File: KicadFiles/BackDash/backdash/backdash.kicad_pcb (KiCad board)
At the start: 2 copper layers, 7 parts

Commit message: need to add in power
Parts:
- removed NANO4: Conn_01x30_Female, TestBaja:arduino_nano
- added REF**: Pin_Header_Straight_1x03_Pitch2.54mm, Pin_Headers:Pin_Header_Straight_1x03_Pitch2.54mm, F.Cu at (231.1, 29.2)
- added REF**: Pin_Header_Straight_1x03_Pitch2.54mm, Pin_Headers:Pin_Header_Straight_1x03_Pitch2.54mm, F.Cu at (219.7, 27.9)
- added REF**: Pin_Header_Straight_1x04_Pitch2.54mm, Pin_Headers:Pin_Header_Straight_1x04_Pitch2.54mm, F.Cu at (247.7, 27.9)
- moved NANO3 188.1 mm to (242.6, 64.8), turned to 270 degrees
- moved NANO2 112.6 mm to (189.2, 50.8), turned to 180 degrees
- moved BUCK1 106.6 mm to (213.4, 41.9), turned to 270 degrees
- moved RTD1 90.7 mm to (193.0, 86.4), turned to 90 degrees
- moved NANO1 80.8 mm to (189.2, 31.8), turned to 180 degrees
- moved CAN1 20.7 mm to (232.4, 86.4), turned to 90 degrees
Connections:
- net /INT renamed Net-(CAN1-Pad10)
- net /RDY renamed Net-(RTD1-Pad8)
- net Net-(BUCK1-Pad3) renamed /IN
- BUCK1 pad 4: Net-(BUCK1-Pad4) -> /GND
- BUCK1 pad 5: Net-(BUCK1-Pad5) -> /VCC
- CAN1 pad 1: /GND -> Net-(CAN1-Pad1)
- CAN1 pad 11: /NC -> Net-(CAN1-Pad11)
- CAN1 pad 12: /NC -> Net-(CAN1-Pad12)
- CAN1 pad 13: /NC -> Net-(CAN1-Pad13)
- CAN1 pad 14: /NC -> Net-(CAN1-Pad14)
- CAN1 pad 2: /3.3V -> /3V3
- CAN1 pad 4: /SDO -> /SDOcan
- CAN1 pad 6: /CS -> /CScan
- CAN1 pad 7: /RST -> Net-(CAN1-Pad7)
- CAN1 pad 8: /NC -> Net-(CAN1-Pad8)
- CAN1 pad 9: /NC -> Net-(CAN1-Pad9)
- NANO1 pad 1: /TX1 -> Net-(NANO1-Pad1)
- NANO1 pad 10: /D7 -> Net-(NANO1-Pad10)
- NANO1 pad 11: /D8 -> Net-(NANO1-Pad11)
- NANO1 pad 12: /D9 -> Net-(NANO1-Pad12)
- NANO1 pad 13: /D10 -> Net-(NANO1-Pad13)
- NANO1 pad 14: /D11 -> Net-(NANO1-Pad14)
- NANO1 pad 15: /D12 -> Net-(NANO1-Pad15)
- NANO1 pad 16: /D13 -> Net-(NANO1-Pad16)
- NANO1 pad 17: /3.3V -> Net-(NANO1-Pad17)
- NANO1 pad 18: /REF -> Net-(NANO1-Pad18)
- NANO1 pad 2: /RX0 -> Net-(NANO1-Pad2)
- NANO1 pad 20: /A1 -> Net-(NANO1-Pad20)
- NANO1 pad 21: /A2 -> Net-(NANO1-Pad21)
- NANO1 pad 22: /A3 -> Net-(NANO1-Pad22)
- NANO1 pad 25: /A6 -> Net-(NANO1-Pad25)
- NANO1 pad 26: /A7 -> Net-(NANO1-Pad26)
- NANO1 pad 28: /RST -> Net-(NANO1-Pad28)
- NANO1 pad 3: /RST -> Net-(NANO1-Pad3)
- NANO1 pad 30: /VIN -> Net-(NANO1-Pad30)
- NANO1 pad 4: /GND -> Net-(NANO1-Pad4)
- NANO1 pad 5: /D2 -> Net-(NANO1-Pad5)
- NANO1 pad 6: /D3 -> Net-(NANO1-Pad6)
- NANO1 pad 7: /D4 -> Net-(NANO1-Pad7)
- NANO1 pad 8: /D5 -> Net-(NANO1-Pad8)
- NANO1 pad 9: /D6 -> Net-(NANO1-Pad9)
- NANO2 pad 1: /TX1 -> Net-(NANO2-Pad1)
- NANO2 pad 10: /D7 -> Net-(NANO2-Pad10)
- NANO2 pad 11: /D8 -> Net-(NANO2-Pad11)
- NANO2 pad 12: /D9 -> /CSrtd
- NANO2 pad 14: /D11 -> /CLK
- NANO2 pad 15: /D12 -> /SDOrtd
- NANO2 pad 16: /D13 -> /CLK
- NANO2 pad 17: /3.3V -> Net-(NANO2-Pad17)
- NANO2 pad 18: /REF -> Net-(NANO2-Pad18)
- NANO2 pad 19: /A0 -> Net-(NANO2-Pad19)
- NANO2 pad 2: /RX0 -> Net-(NANO2-Pad2)
- NANO2 pad 20: /A1 -> Net-(NANO2-Pad20)
- NANO2 pad 21: /A2 -> Net-(NANO2-Pad21)
- NANO2 pad 22: /A3 -> Net-(NANO2-Pad22)
- NANO2 pad 25: /A6 -> Net-(NANO2-Pad25)
- NANO2 pad 26: /A7 -> Net-(NANO2-Pad26)
- NANO2 pad 28: /RST -> Net-(NANO2-Pad28)
- NANO2 pad 3: /RST -> Net-(NANO2-Pad3)
- NANO2 pad 30: /VIN -> Net-(NANO2-Pad30)
- NANO2 pad 4: /GND -> Net-(NANO2-Pad4)
- NANO2 pad 5: /D2 -> Net-(NANO2-Pad5)
- NANO2 pad 6: /D3 -> Net-(NANO2-Pad6)
- NANO2 pad 7: /D4 -> Net-(NANO2-Pad7)
- NANO2 pad 8: /D5 -> Net-(NANO2-Pad8)
- NANO2 pad 9: /D6 -> Net-(NANO2-Pad9)
- NANO3 pad 1: /TX1 -> Net-(NANO3-Pad1)
- NANO3 pad 10: /D7 -> Net-(NANO3-Pad10)
- NANO3 pad 11: /D8 -> Net-(NANO3-Pad11)
- NANO3 pad 12: /D9 -> Net-(NANO3-Pad12)
- NANO3 pad 13: /D10 -> /CScan
- NANO3 pad 14: /D11 -> /SDI
- NANO3 pad 15: /D12 -> /SDOcan
- NANO3 pad 16: /D13 -> /SCK
- NANO3 pad 17: /3.3V -> Net-(NANO3-Pad17)
- NANO3 pad 18: /REF -> Net-(NANO3-Pad18)
- NANO3 pad 19: /A0 -> Net-(NANO3-Pad19)
- NANO3 pad 2: /RX0 -> Net-(NANO3-Pad2)
- NANO3 pad 20: /A1 -> Net-(NANO3-Pad20)
- NANO3 pad 21: /A2 -> Net-(NANO3-Pad21)
- NANO3 pad 22: /A3 -> Net-(NANO3-Pad22)
- NANO3 pad 25: /A6 -> Net-(NANO3-Pad25)
- NANO3 pad 26: /A7 -> Net-(NANO3-Pad26)
- NANO3 pad 28: /RST -> Net-(NANO3-Pad28)
- NANO3 pad 3: /RST -> Net-(NANO3-Pad3)
- NANO3 pad 30: /VIN -> Net-(NANO3-Pad30)
- NANO3 pad 4: /GND -> Net-(NANO3-Pad4)
- NANO3 pad 5: /D2 -> Net-(NANO3-Pad5)
- NANO3 pad 6: /D3 -> Net-(NANO3-Pad6)
- NANO3 pad 7: /D4 -> Net-(NANO3-Pad7)
- NANO3 pad 8: /D5 -> Net-(NANO3-Pad8)
- NANO3 pad 9: /D6 -> Net-(NANO3-Pad9)
- RTD1 pad 3: /3V3 -> Net-(RTD1-Pad3)
- RTD1 pad 5: /SDO -> /SDOrtd
- RTD1 pad 7: /CS -> /CSrtd
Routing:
- net /VCC: track 0.00 -> 169.4 mm
- net /A4: track 0.00 -> 124.9 mm
- net /A5: track 0.00 -> 115.6 mm
- net /SDI: track 0.00 -> 67.3 mm
- net /CLK: track 0.00 -> 52.4 mm
- net /GND: track 0.00 -> 52.0 mm
- net /A0: track 0.00 -> 44.3 mm
- net /SDOrtd: track 0.00 -> 39.4 mm
- net /SCK: track 0.00 -> 36.0 mm
- net /CSrtd: track 0.00 -> 29.0 mm
- net /CScan: track 0.00 -> 22.2 mm
- net /SDOcan: track 0.00 -> 15.0 mm
- added copper zone on B.Cu, net /GND
- added copper zone on F.Cu, net /VCC
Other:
- board outline added: 91.4 x 67.3 mm
- net class Default: trace_width 0.25 -> 0.508
- board text added: "cvt"
- board text added: "tach"

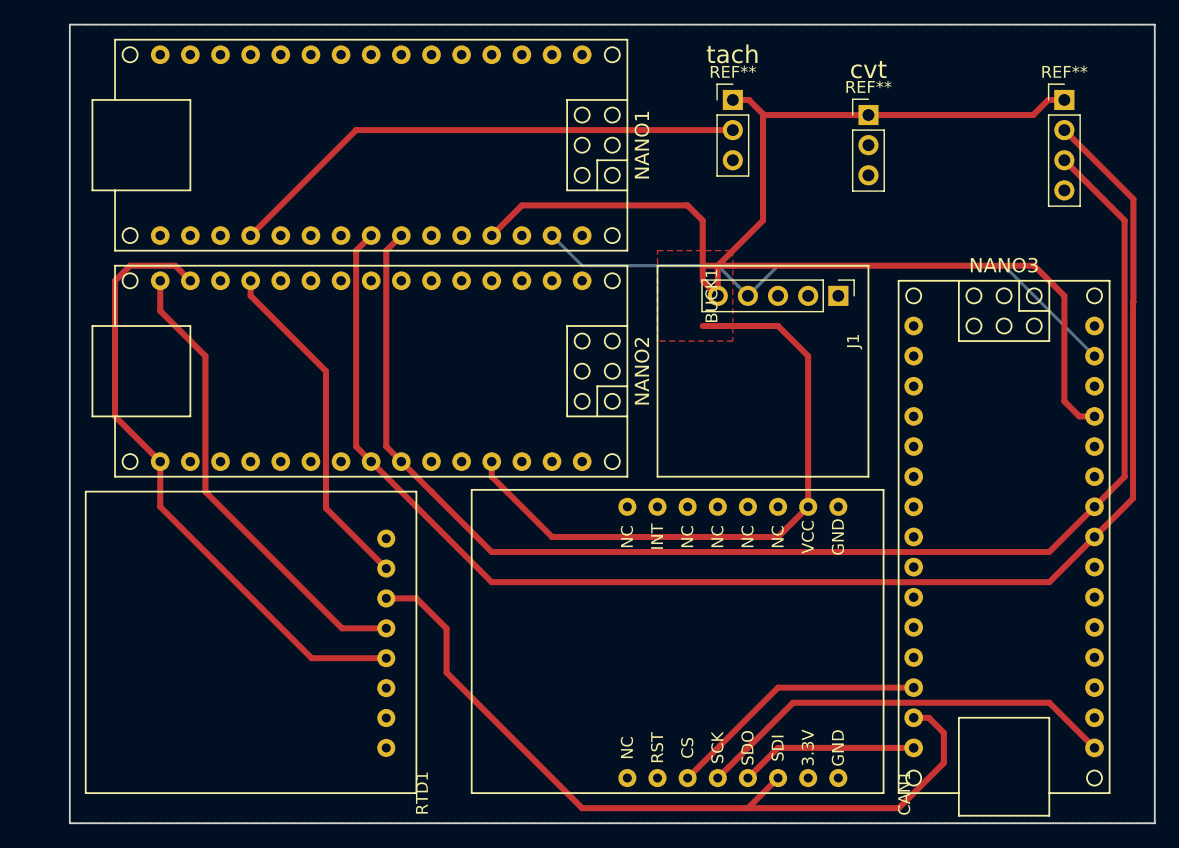
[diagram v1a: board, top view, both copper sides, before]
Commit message: logo and batt added
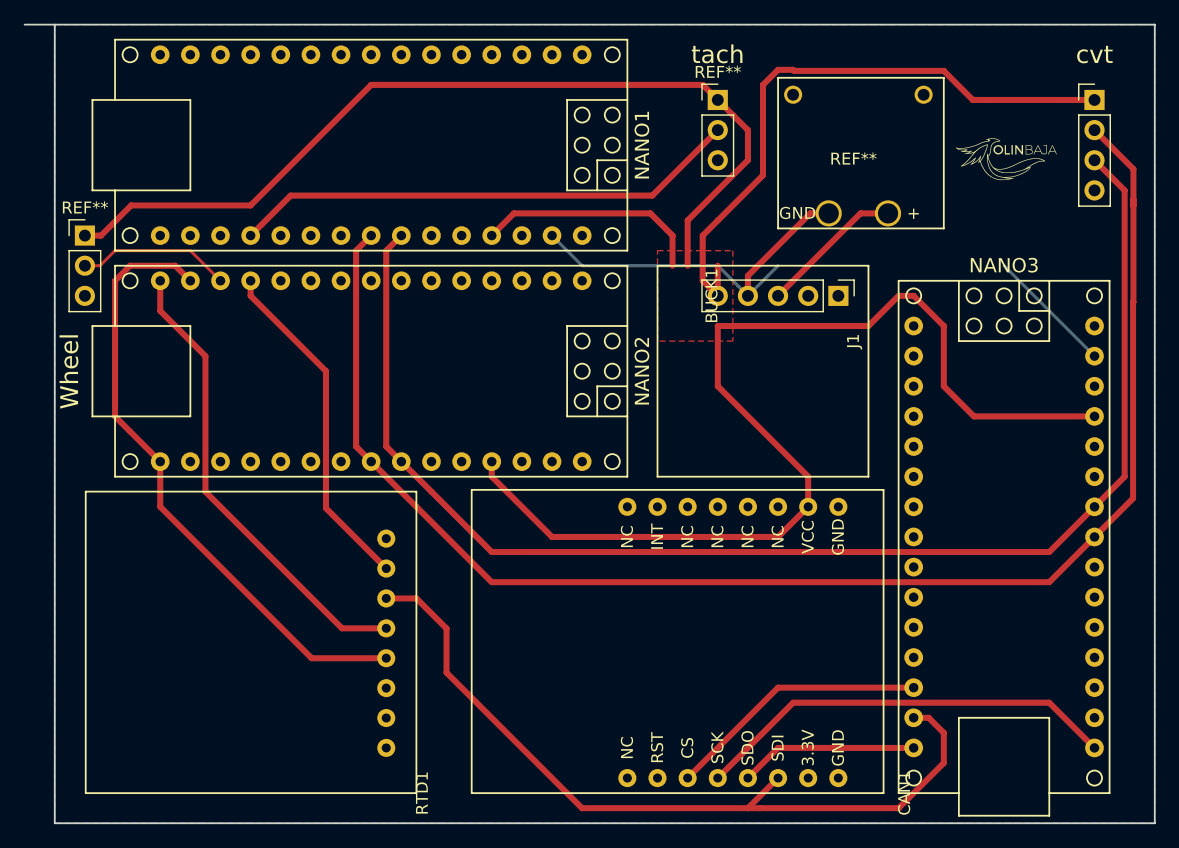
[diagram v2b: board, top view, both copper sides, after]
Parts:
- added G***: LOGO, TestBaja:Baja_Logo_Tach, F.Cu at (243.8, 33.0)
- added REF**: DC_Connector, TestBaja:DC_Connector, F.Cu at (224.8, 37.5)
- moved REF** 66.8 mm to (165.1, 39.4)
- moved REF** 2.54 mm to (250.2, 27.9)
- moved REF** 1.27 mm to (218.4, 27.9)
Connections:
- REF** pad 2: (no net) -> /D10
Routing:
- net /VCC: track 169.4 -> 237.5 mm
- net /D10: track 0.00 -> 13.0 mm
- net /IN: track 0.00 -> 12.1 mm
- net /GND: track 52.0 -> 43.7 mm
- net /A0: track 44.3 -> 43.1 mm
- net /A5: track 115.6 -> 114.6 mm
- net /A4: track 124.9 -> 124.4 mm
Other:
- board size 91.4 x 67.3 mm -> 95.2 x 67.3 mm
- board text added: "Wheel"

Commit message: Board edge was a little off
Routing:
- net /CLK: track 52.4 -> 53.7 mm
- net /D10: track 13.0 -> 14.0 mm
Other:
- board size 95.2 x 67.3 mm -> 92.7 x 67.3 mm
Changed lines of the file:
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@@
-(kicad_pcb (version 20171130) (host pcbnew 6.0.0-rc1-unknown-7c960aa~66~ubuntu18.04.1)
+(kicad_pcb (version 20171130) (host pcbnew "(5.0.0)")
   (general
     (thickness 1.6)
     (drawings 7)
-    (tracks 126)
+    (tracks 129)
     (zones 0)
     (modules 11)
@@
     (zone_45_only no)
     (trace_min 0.2)
+    (segment_width 0.2)
+    (edge_width 0.15)
     (via_size 0.8)
     (via_drill 0.4)
@@
     (uvia_min_size 0.2)
     (uvia_min_drill 0.1)
-    (edge_width 0.15)
-    (segment_width 0.2)
     (pcb_text_width 0.3)
     (pcb_text_size 1.5 1.5)
@@
     (pcbplotparams
       (layerselection 0x010fc_ffffffff)
-      (usegerberextensions false)
+      (usegerberextensions true)
       (usegerberattributes false)
       (usegerberadvancedattributes false)
@@
       (outputformat 1)
       (mirror false)
-      (drillshape 1)
+      (drillshape 0)
       (scaleselection 1)
-      (outputdirectory ""))
+      (outputdirectory "../../BackDashv1_gerbers/"))
   )
   (net 0 "")
@@
   (gr_line (start 255.27 88.9) (end 162.56 88.9) (layer Edge.Cuts) (width 0.15))
   (gr_line (start 255.27 21.59) (end 255.27 88.9) (layer Edge.Cuts) (width 0.15))
-  (gr_line (start 160.02 21.59) (end 255.27 21.59) (layer Edge.Cuts) (width 0.15))
+  (gr_line (start 162.56 21.59) (end 255.27 21.59) (layer Edge.Cuts) (width 0.15))
   (segment (start 220.130001 43.600001) (end 220.98 44.45) (width 0.25) (layer B.Cu) (net 2))
   (segment (start 218.44 41.91) (end 220.130001 43.600001) (width 0.25) (layer B.Cu) (net 2))
@@
   (segment (start 218.44 30.48) (end 212.92 36) (width 0.508) (layer F.Cu) (net 6))
   (segment (start 212.92 36) (end 182.44 36) (width 0.508) (layer F.Cu) (net 6))
-  (segment (start 176.53 43.18) (end 173.99 40.64) (width 0.25) (layer F.Cu) (net 7))
-  (segment (start 173.99 40.64) (end 167.64 40.64) (width 0.25) (layer F.Cu) (net 7))
-  (segment (start 167.64 40.64) (end 166.37 41.91) (width 0.25) (layer F.Cu) (net 7))
+  (segment (start 173.99 41.021) (end 167.64 41.021) (width 0.25) (layer F.Cu) (net 7))
   (segment (start 166.37 41.91) (end 165.1 41.91) (width 0.25) (layer F.Cu) (net 7))
-  (segment (start 168.91 41.91) (end 167.64 43.18) (width 0.508) (layer F.Cu) (net 9))
-  (segment (start 171.45 58.42) (end 168.91 55.88) (width 0.508) (layer F.Cu) (net 9))
-  (segment (start 168.91 55.88) (end 167.64 54.61) (width 0.508) (layer F.Cu) (net 9))
-  (segment (start 167.64 54.61) (end 167.64 43.18) (width 0.508) (layer F.Cu) (net 9))
+  (segment (start 174.371 41.021) (end 173.99 41.021) (width 0.508) (layer F.Cu) (net 7))
+  (segment (start 176.53 43.18) (end 174.371 41.021) (width 0.508) (layer F.Cu) (net 7))
+  (segment (start 167.191081 41.021) (end 167.64 41.021) (width 0.508) (layer F.Cu) (net 7))
+  (segment (start 166.302081 41.91) (end 167.191081 41.021) (width 0.508) (layer F.Cu) (net 7))
+  (segment (start 165.1 41.91) (end 166.302081 41.91) (width 0.508) (layer F.Cu) (net 7))
   (segment (start 184.21 74.99) (end 171.45 62.23) (width 0.508) (layer F.Cu) (net 9))
   (segment (start 171.45 62.23) (end 171.45 58.42) (width 0.508) (layer F.Cu) (net 9))
-  (segment (start 173.99 43.18) (end 172.72 41.91) (width 0.508) (layer F.Cu) (net 9))
   (segment (start 190.5 74.99) (end 184.21 74.99) (width 0.508) (layer F.Cu) (net 9))
-  (segment (start 172.72 41.91) (end 168.91 41.91) (width 0.508) (layer F.Cu) (net 9))
+  (segment (start 173.99 42.066449) (end 173.99 43.18) (width 0.508) (layer F.Cu) (net 9))
+  (segment (start 173.579551 41.656) (end 173.99 42.066449) (width 0.508) (layer F.Cu) (net 9))
+  (segment (start 168.275 41.656) (end 173.579551 41.656) (width 0.508) (layer F.Cu) (net 9))
+  (segment (start 167.64 42.291) (end 168.275 41.656) (width 0.508) (layer F.Cu) (net 9))
+  (segment (start 167.64 54.61) (end 167.64 42.291) (width 0.508) (layer F.Cu) (net 9))
+  (segment (start 171.45 58.42) (end 167.64 54.61) (width 0.508) (layer F.Cu) (net 9))
   (segment (start 234.95 80.01) (end 236.22 80.01) (width 0.508) (layer F.Cu) (net 10))
   (segment (start 236.22 80.01) (end 237.49 81.28) (width 0.508) (layer F.Cu) (net 10))
